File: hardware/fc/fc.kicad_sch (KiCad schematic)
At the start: 31 parts, among them SW1 Push, U12 RP2354A, X1 ABM8-272-T3

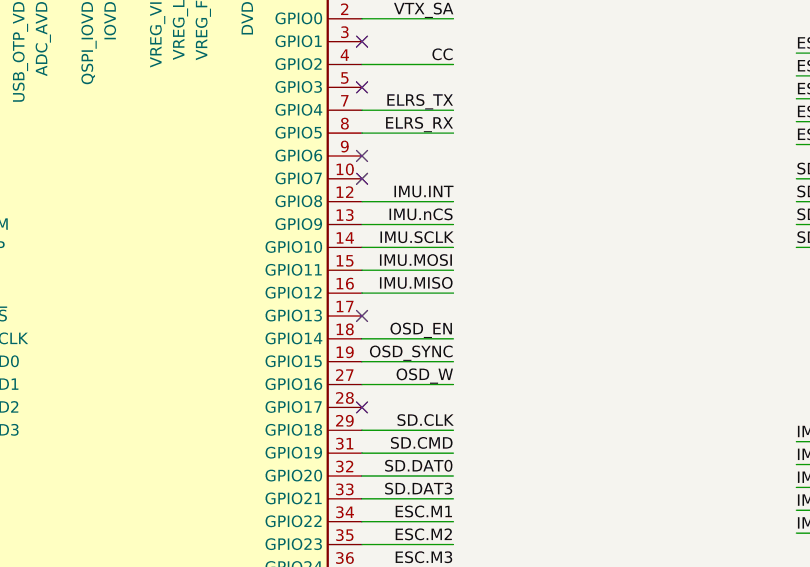
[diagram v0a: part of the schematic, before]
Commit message: fc: prelim MCU and IMU layout
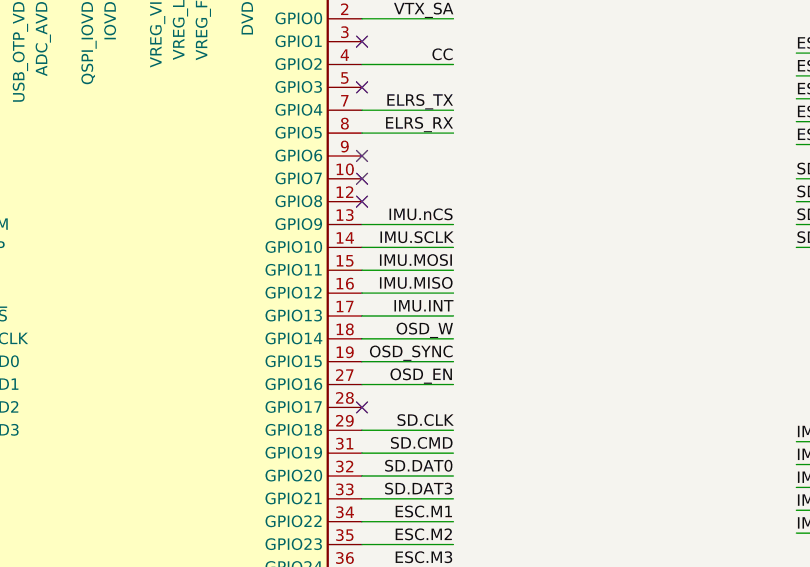
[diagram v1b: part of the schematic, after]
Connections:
- net IMU.INT: now also U12.17 (GPIO13); no longer U12.12 (GPIO8)
- net OSD_EN: now also U12.27 (GPIO16); no longer U12.18 (GPIO14)
- net OSD_W: now also U12.18 (GPIO14); no longer U12.27 (GPIO16)
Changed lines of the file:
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@@
+	)
+	(no_connect
+		(at 128.27 109.22)
 	)
 	(no_connect
@@
 	(no_connect
 		(at 77.47 134.62)
-	)
-	(no_connect
-		(at 128.27 121.92)
 	)
 	(no_connect
@@
 	(wire
 		(pts
-			(xy 128.27 109.22) (xy 138.43 109.22)
-		)
-		(stroke
-			(width 0)
-			(type default)
-		)
-	)
-	(wire
-		(pts
 			(xy 186.69 102.87) (xy 176.53 102.87)
 		)
@@
 		(pts
 			(xy 104.14 40.64) (xy 104.14 43.18)
+		)
+		(stroke
+			(width 0)
+			(type default)
+		)
+	)
+	(wire
+		(pts
+			(xy 128.27 121.92) (xy 138.43 121.92)
 		)
 		(stroke
@@
 		)
 	)
-	(label "OSD_EN"
+	(label "OSD_W"
 		(at 138.43 124.46 180)
 		(effects
@@
 		)
 	)
-	(label "OSD_W"
+	(label "OSD_EN"
 		(at 138.43 129.54 180)
 		(effects
@@
 	)
 	(label "IMU.INT"
-		(at 138.43 109.22 180)
-		(effects
-			(font
+		(at 138.43 121.92 180)
+		(effects
+			(font

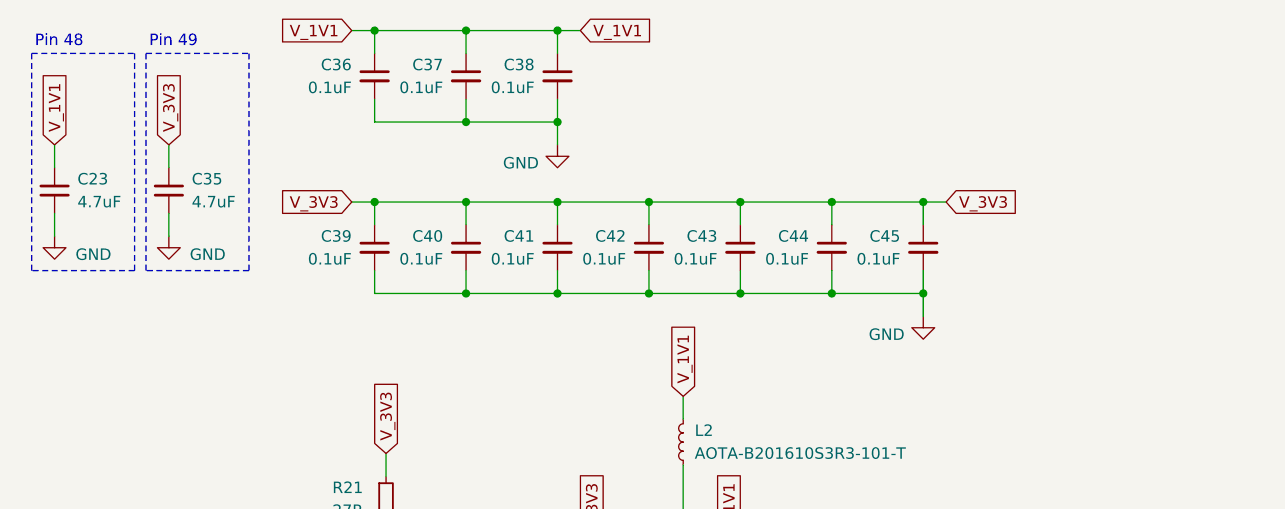
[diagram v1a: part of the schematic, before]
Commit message: fc: prelim MCU + IMU
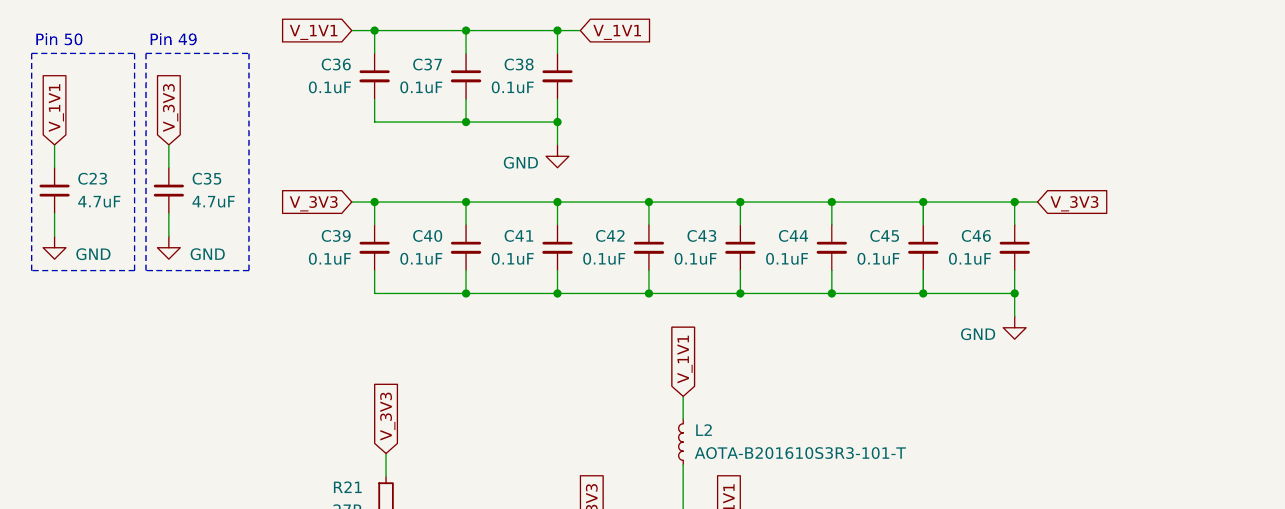
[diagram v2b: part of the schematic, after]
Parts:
- added C46: 0.1uF, Stratus:C_0402, symbol Device:C_Small
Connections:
- net GND: now also C46.2
- net V_3V3: now also C46.1
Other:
- note added: "Pin 50"
- note removed: "Pin 48"
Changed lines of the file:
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@@
 		)
 	)
-	(text "Pin 48\n"
+	(text "Pin 50"
 		(exclude_from_sim no)
 		(at 38.608 22.86 0)
@@
 	)
 	(junction
+		(at 144.78 50.8)
+		(diameter 0)
+		(color 0 0 0 0)
+	)
+	(junction
+		(at 144.78 40.64)
+		(diameter 0)
+		(color 0 0 0 0)
+	)
+	(junction
 		(at 83.82 40.64)
 		(diameter 0)
@@
 	(wire
 		(pts
+			(xy 144.78 50.8) (xy 144.78 48.26)
+		)
+		(stroke
+			(width 0)
+			(type default)
+		)
+	)
+	(wire
+		(pts
 			(xy 67.31 160.02) (xy 77.47 160.02)
 		)
@@
 	(wire
 		(pts
+			(xy 144.78 50.8) (xy 134.62 50.8)
+		)
+		(stroke
+			(width 0)
+			(type default)
+		)
+	)
+	(wire
+		(pts
 			(xy 128.27 88.9) (xy 138.43 88.9)
 		)
@@
 	(wire
 		(pts
+			(xy 144.78 40.64) (xy 147.32 40.64)
+		)
+		(stroke
+			(width 0)
+			(type default)
+		)
+	)
+	(wire
+		(pts
 			(xy 267.97 97.79) (xy 278.13 97.79)
 		)
@@
 	(wire
 		(pts
+			(xy 144.78 40.64) (xy 144.78 43.18)
+		)
+		(stroke
+			(width 0)
+			(type default)
+		)
+	)
+	(wire
+		(pts
 			(xy 83.82 40.64) (xy 93.98 40.64)
 		)
@@
 	(wire
 		(pts
-			(xy 134.62 40.64) (xy 137.16 40.64)
+			(xy 134.62 40.64) (xy 144.78 40.64)
 		)
 		(stroke
@@
 	(wire
 		(pts
-			(xy 134.62 53.34) (xy 134.62 50.8)
+			(xy 144.78 53.34) (xy 144.78 50.8)
 		)
 		(stroke
@@
 	(global_label "V_3V3"
 		(shape input)
-		(at 137.16 40.64 0)
+		(at 147.32 40.64 0)
 		(fields_autoplaced yes)
 		(effects
@@
 		)
 		(property "Intersheetrefs" "${INTERSHEET_REFS}"
-			(at 145.709 40.64 0)
+			(at 155.869 40.64 0)
 			(hide yes)
 			(show_name no)
@@
 	)
 	(symbol
+		(lib_name "C_Small_2")
+		(lib_id "Device:C_Small")
+		(at 144.78 45.72 0)
+		(mirror y)
+		(unit 1)
+		(body_style 1)
+		(exclude_from_sim no)
+		(in_bom yes)
+		(on_board yes)
+		(in_pos_files yes)
+		(dnp no)
+		(property "Reference" "C46"
+			(at 142.24 44.4562 0)
+			(show_name no)
+			(do_not_autoplace no)
+			(effects
+				(font
+					(size 1.27 1.27)
+				)
+				(justify left)
+			)
+		)
+		(property "Value" "0.1uF"
+			(at 142.24 46.9962 0)
+			(show_name no)
+			(do_not_autoplace no)
+			(effects
+				(font
+					(size 1.27 1.27)
+				)
+				(justify left)
+			)
+		)
+		(property "Footprint" "Stratus:C_0402"
+			(at 144.78 45.72 0)
+			(hide yes)
+			(show_name no)
+			(do_not_autoplace no)
+			(effects
+				(font
+					(size 1.27 1.27)
+				)
+			)
+		)
+		(property "Datasheet" ""
+			(at 144.78 45.72 0)
+			(hide yes)
+			(show_name no)
+			(do_not_autoplace no)
+			(effects
+				(font
+					(size 1.27 1.27)
+				)
+			)
+		)
+		(property "Description" "Unpolarized capacitor, small symbol"
+			(at 144.78 45.72 0)
+			(hide yes)
+			(show_name no)
+			(do_not_autoplace no)
+			(effects
+				(font
+					(size 1.27 1.27)
+				)
+			)
+		)
+		(pin "2"
+		)
+		(pin "1"
+		)
+		(instances
+			(project "fc"
+				(path "/6eb6d89e-9d71-4347-9ba3-a394c00e5720"
+					(reference "C46")
+					(unit 1)
+				)
+			)
+		)
+	)
+	(symbol
 		(lib_id "power:GND")
-		(at 134.62 53.34 0)
+		(at 144.78 53.34 0)
 		(mirror y)
 		(unit 1)
@@
 		(dnp no)
 		(property "Reference" "#PWR055"
-			(at 134.62 59.69 0)
+			(at 144.78 59.69 0)
 			(hide yes)
 			(show_name no)
@@
 		)
 		(property "Value" "GND"
-			(at 130.556 55.372 0)
+			(at 140.716 55.372 0)
 			(show_name no)
 			(do_not_autoplace no)
@@
 		)
 		(property "Footprint" ""
-			(at 134.62 53.34 0)
+			(at 144.78 53.34 0)
 			(hide yes)
 			(show_name no)
@@
 		)
 		(property "Datasheet" ""
-			(at 134.62 53.34 0)
+			(at 144.78 53.34 0)
 			(hide yes)
 			(show_name no)
@@
 		)
 		(property "Description" "Power symbol creates a global label with name \"GND\" , ground"
-			(at 134.62 53.34 0)
+			(at 144.78 53.34 0)
 			(hide yes)
 			(show_name no)

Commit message: fc: routing and pours
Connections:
- net ESC.TEL: now also U12.2 (GPIO0)
- net VTX_SA: now also U12.5 (GPIO3); no longer U12.2 (GPIO0)
- no-connect marks 14 -> 13
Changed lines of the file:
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@@
-	)
-	(no_connect
-		(at 128.27 96.52)
 	)
 	(no_connect
@@
 	(wire
 		(pts
+			(xy 144.78 40.64) (xy 147.32 40.64)
+		)
+		(stroke
+			(width 0)
+			(type default)
+		)
+	)
+	(wire
+		(pts
 			(xy 128.27 88.9) (xy 138.43 88.9)
 		)
@@
 	(wire
 		(pts
-			(xy 144.78 40.64) (xy 147.32 40.64)
-		)
-		(stroke
-			(width 0)
-			(type default)
-		)
-	)
-	(wire
-		(pts
 			(xy 267.97 97.79) (xy 278.13 97.79)
 		)
@@
 		(pts
 			(xy 128.27 99.06) (xy 138.43 99.06)
+		)
+		(stroke
+			(width 0)
+			(type default)
+		)
+	)
+	(wire
+		(pts
+			(xy 128.27 96.52) (xy 138.43 96.52)
 		)
 		(stroke
@@
 		)
 	)
+	(label "ESC.TEL"
+		(at 138.43 88.9 180)
+		(effects
+			(font
+				(size 1.27 1.27)
+			)
+			(justify right bottom)
+		)
+	)
 	(label "ESC.M4"
 		(at 176.53 100.33 0)
@@
 		)
 	)
-	(label "VTX_SA"
-		(at 138.43 88.9 180)
-		(effects
-			(font
-				(size 1.27 1.27)
-			)
-			(justify right bottom)
-		)
-	)
 	(label "IMU.nCS"
 		(at 138.43 111.76 180)
@@
 		(effects
 			(font
+				(size 1.27 1.27)
+			)
+			(justify right bottom)
+		)
+	)
+	(label "VTX_SA"
+		(at 138.43 96.52 180)
+		(effects
+			(font

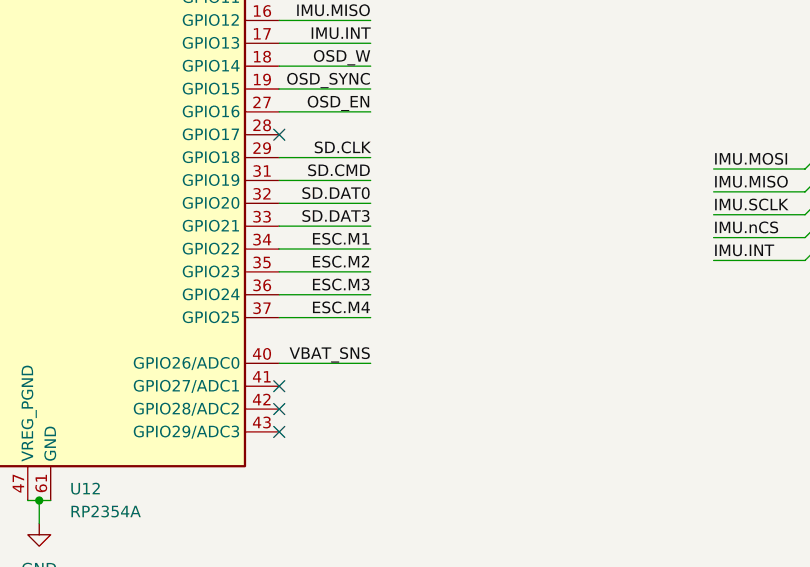
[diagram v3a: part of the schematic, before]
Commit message: fc: add dshot resistors
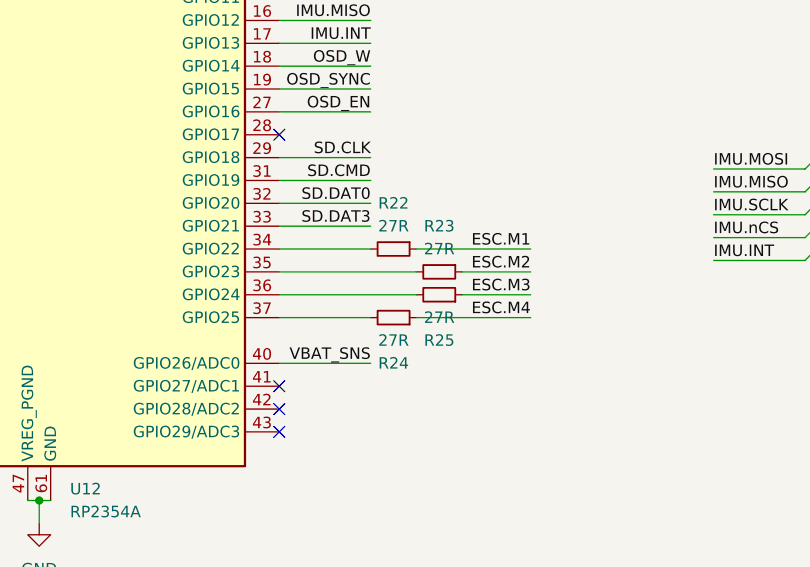
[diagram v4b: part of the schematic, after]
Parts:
- added R22, R23, R24, R25: 27R, Stratus:R_0402, symbol Device:R_Small
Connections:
- net ESC.M1: now also R22.1; no longer U12.34 (GPIO22)
- net ESC.M2: now also R23.1; no longer U12.35 (GPIO23)
- net ESC.M3: now also R25.1; no longer U12.36 (GPIO24)
- net ESC.M4: now also R24.1; no longer U12.37 (GPIO25)
- new net: R22.2, U12.34 (GPIO22)
- new net: R23.2, U12.35 (GPIO23)
- new net: R25.2, U12.36 (GPIO24)
- new net: R24.2, U12.37 (GPIO25)

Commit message: fc: footprints
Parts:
- H1, H2, H3, H4: footprint MountingHole:MountingHole_3.2mm_M3 -> Stratus:Mount_M3_K0.5
- U12: footprint Package_DFN_QFN:QFN-60-1EP_7x7mm_P0.4mm_EP3.4x3.4mm -> Stratus:RP2354A
- X1: footprint PCM_Crystal_AKL:Crystal_SMD_3225-4Pin_3.2x2.5mm -> Stratus:Crystal_4P_3.2x2.5mm
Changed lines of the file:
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@@
 			)
 		)
-		(property "Footprint" "Package_DFN_QFN:QFN-60-1EP_7x7mm_P0.4mm_EP3.4x3.4mm"
+		(property "Footprint" "Stratus:RP2354A"
 			(at 102.87 127 0)
 			(hide yes)
@@
 			)
 		)
-		(property "Footprint" "PCM_Crystal_AKL:Crystal_SMD_3225-4Pin_3.2x2.5mm"
+		(property "Footprint" "Stratus:Crystal_4P_3.2x2.5mm"
 			(at 60.96 147.32 0)
 			(hide yes)
@@
 			)
 		)
-		(property "Footprint" "MountingHole:MountingHole_3.2mm_M3"
+		(property "Footprint" "Stratus:Mount_M3_K0.5"
 			(at 237.49 25.4 0)
 			(hide yes)
@@
 			)
 		)
-		(property "Footprint" "MountingHole:MountingHole_3.2mm_M3"
+		(property "Footprint" "Stratus:Mount_M3_K0.5"
 			(at 248.92 25.4 0)
 			(hide yes)
@@
 			)
 		)
-		(property "Footprint" "MountingHole:MountingHole_3.2mm_M3"
+		(property "Footprint" "Stratus:Mount_M3_K0.5"
 			(at 271.78 25.4 0)
 			(hide yes)
@@
 			)
 		)
-		(property "Footprint" "MountingHole:MountingHole_3.2mm_M3"
+		(property "Footprint" "Stratus:Mount_M3_K0.5"
 			(at 260.35 25.4 0)
 			(hide yes)

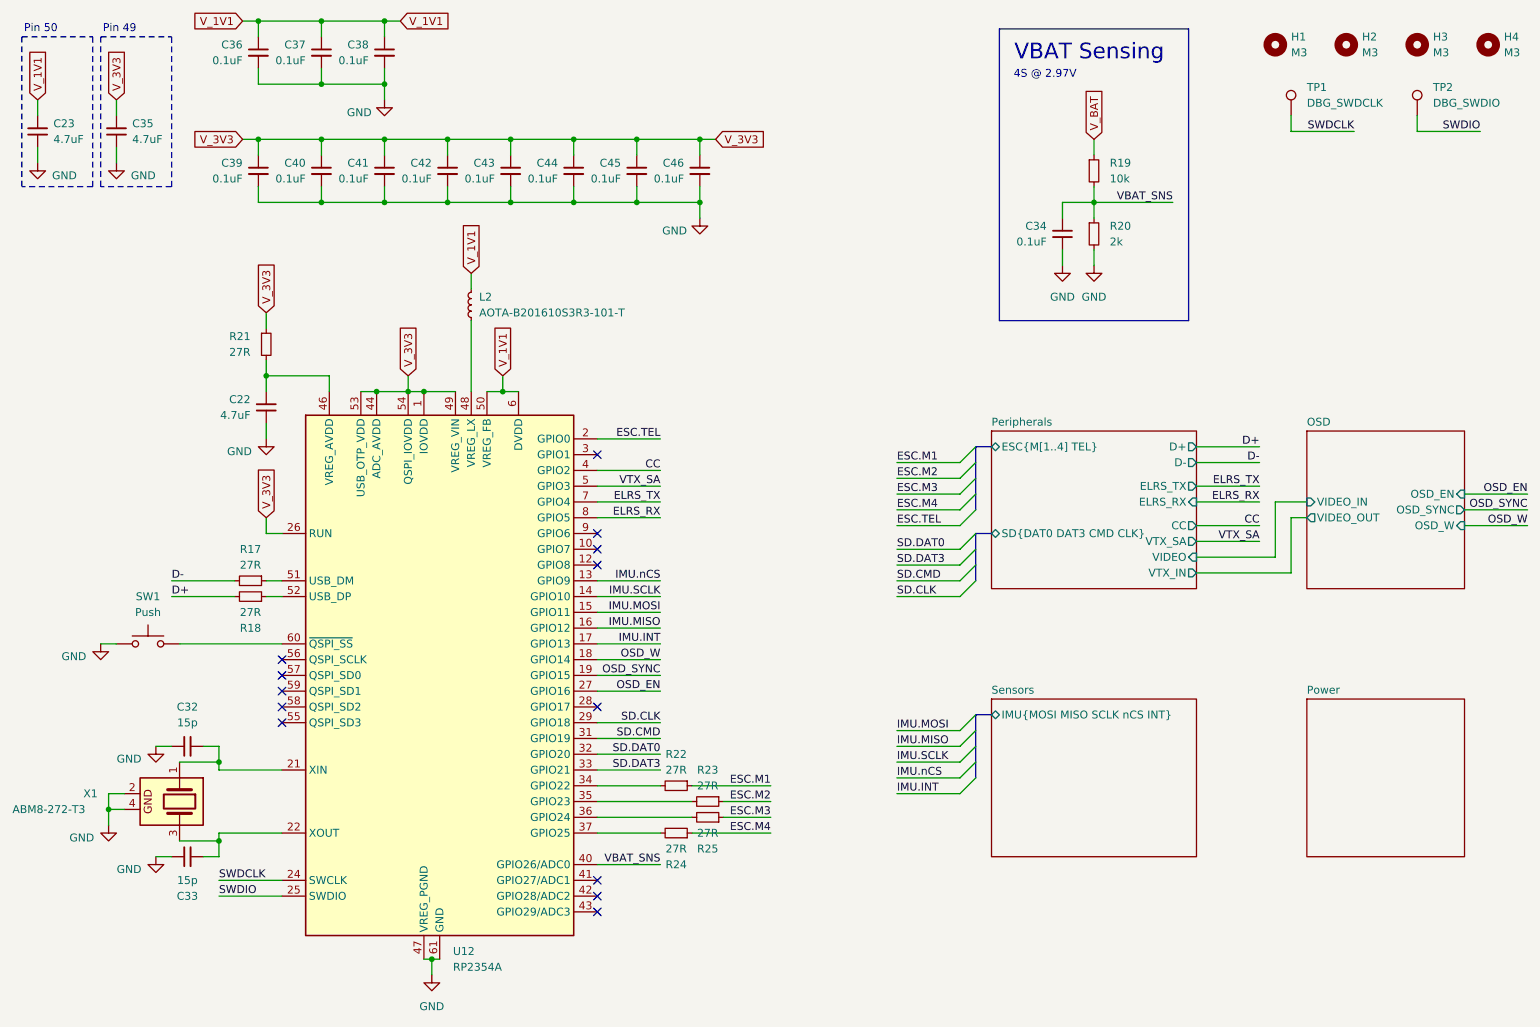
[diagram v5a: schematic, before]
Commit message: fc: add LEDs
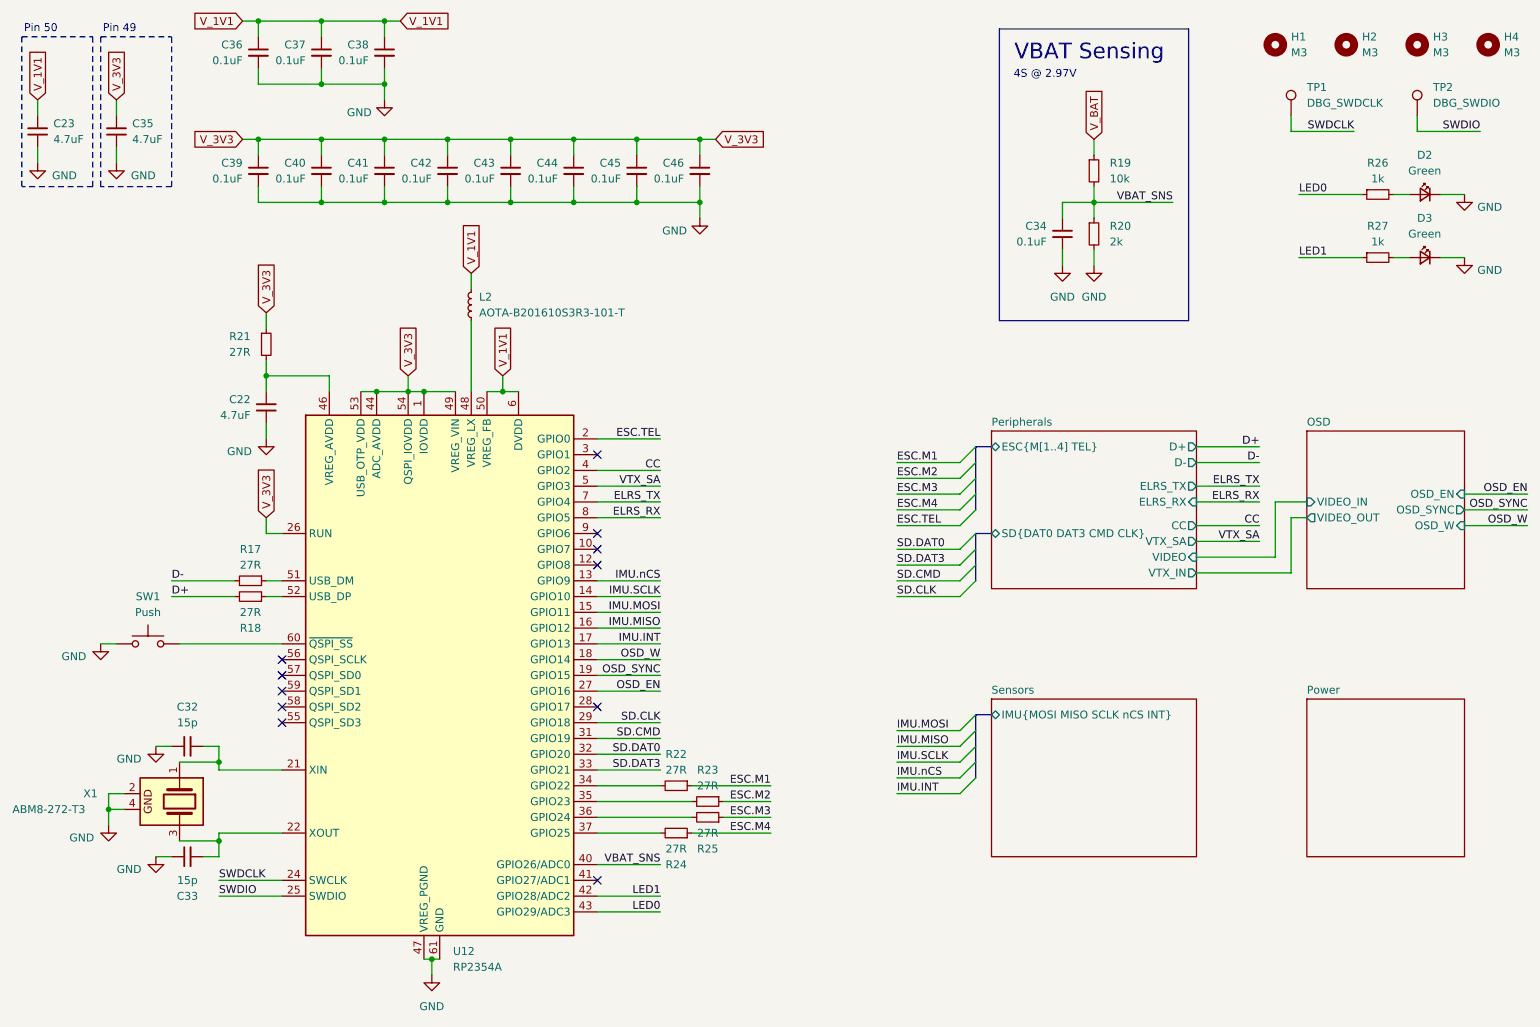
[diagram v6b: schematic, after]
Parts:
- added D2, D3: Green, LED_SMD:LED_0603_1608Metric, symbol Device:LED_Small
- added R26, R27: 1k, Stratus:R_0402, symbol Device:R_Small
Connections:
- net GND: now also D2.1 (K), D3.1 (K)
- net LED1: now reaches U12.42 (GPIO28/ADC2)
- net LED1: now also R27.1
- net LED0: now reaches U12.43 (GPIO29/ADC3)
- net LED0: now also R26.1
- new net: D2.2 (A), R26.2
- new net: D3.2 (A), R27.2
- no-connect marks 13 -> 11
